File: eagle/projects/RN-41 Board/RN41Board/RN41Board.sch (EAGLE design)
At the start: 16 parts, among them J1 640456-5, Q1 MOSFET-NCHANNELSMD, U1 BLUETOOTH-RN41, U3 3.3V

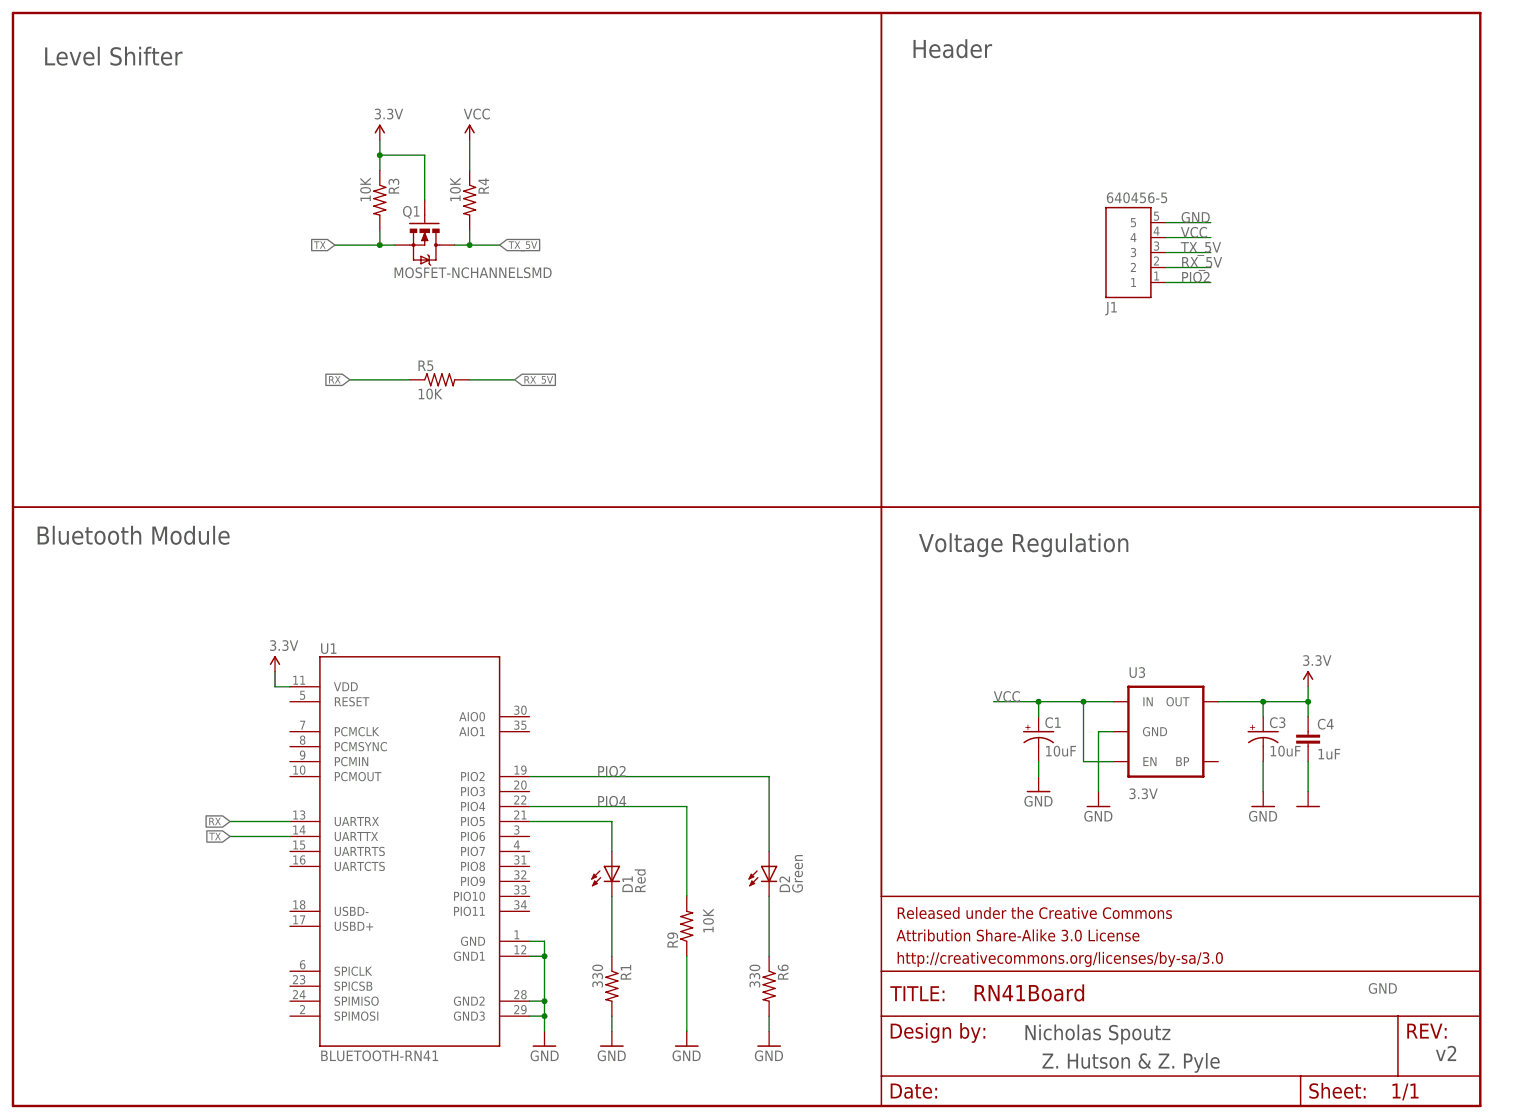
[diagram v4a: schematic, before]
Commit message: OSHPark .dru and RN-41 Update
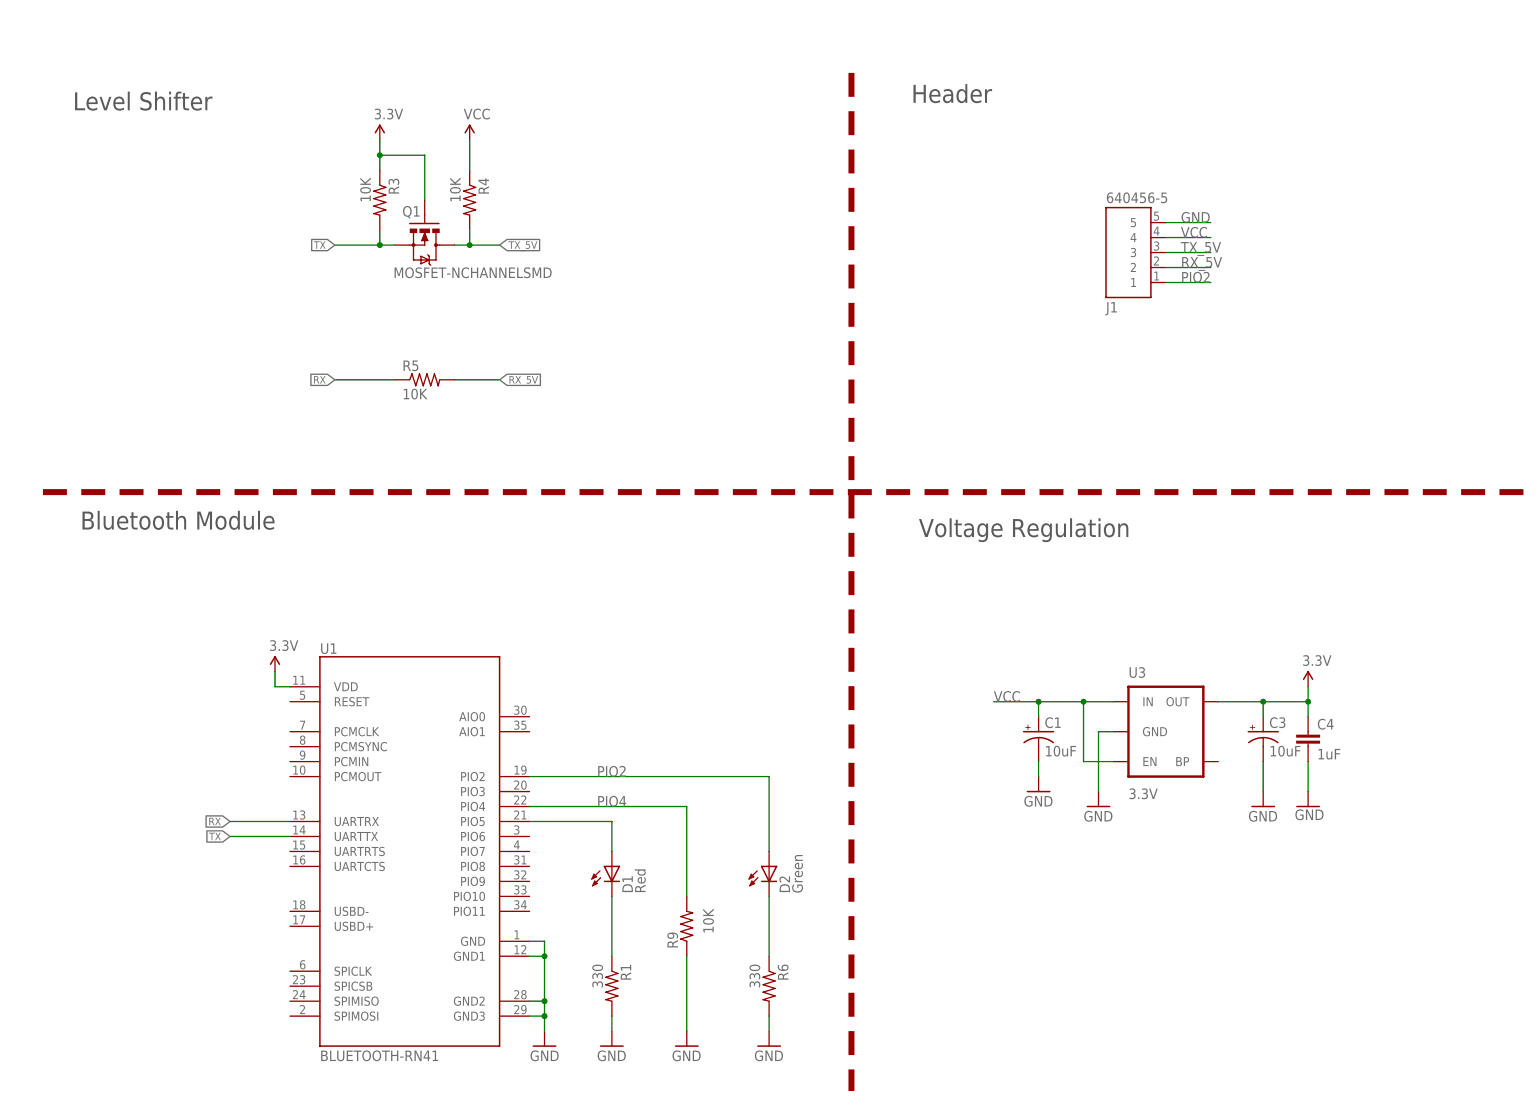
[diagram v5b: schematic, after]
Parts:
- removed FRAME1: FRAME-LETTER, SparkFun-Aesthetics:FRAME-LETTER
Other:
- note removed: "Nicholas Spoutz"
- note removed: "Z. Hutson & Z. Pyle"
- note removed: "v2"
- moved on the sheet: R5
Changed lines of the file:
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@@
 <?xml version="1.0" encoding="utf-8"?>
 <!DOCTYPE eagle SYSTEM "eagle.dtd">
-<eagle version="9.3.0">
+<eagle version="9.3.1">
 <drawing>
 <settings>
@@
 <setting verticaltext="up"/>
 </settings>
-<grid distance="0.1" unitdist="inch" unit="inch" style="lines" multiple="1" display="no" altdistance="0.01" altunitdist="inch" altunit="inch"/>
+<grid distance="0.1" unitdist="inch" unit="inch" style="lines" multiple="1" display="yes" altdistance="0.01" altunitdist="inch" altunit="inch"/>
 <layers>
 <layer number="1" name="Top" color="4" fill="1" visible="no" active="no"/>
@@
 </classes>
 <parts>
-<part name="FRAME1" library="SparkFun-Aesthetics" deviceset="FRAME-LETTER" device=""/>
 <part name="C4" library="SparkFun" deviceset="CAP" device="0603-CAP" value="1uF"/>
 <part name="GND1" library="SparkFun" deviceset="GND" device=""/>
@@
 <part name="GND8" library="SparkFun" deviceset="GND" device=""/>
 <part name="J1" library="640456-5" deviceset="640456-5" device=""/>
+<part name="FRAME2" library="frames" library_urn="urn:adsk.eagle:library:229" deviceset="A4L-LOC" device=""/>
 </parts>
 <sheets>
 <sheet>
 <plain>
-<text x="5.08" y="176.53" size="3.048" layer="97">Level Shifter</text>
-<text x="152.4" y="177.8" size="3.048" layer="97">Header</text>
-<text x="171.45" y="11.176" size="2.54" layer="97">Nicholas Spoutz</text>
-<text x="241.3" y="7.62" size="2.54" layer="97">v2</text>
-<text x="174.498" y="6.35" size="2.54" layer="97">Z. Hutson &amp; Z. Pyle</text>
-<wire x1="0" y1="101.6" x2="248.92" y2="101.6" width="0.3048" layer="94"/>
-<wire x1="147.32" y1="35.56" x2="147.32" y2="185.42" width="0.3048" layer="94"/>
-<text x="153.67" y="93.98" size="3.048" layer="97">Voltage Regulation</text>
-<text x="3.81" y="95.25" size="3.048" layer="97">Bluetooth Module</text>
+<text x="10.16" y="168.91" size="3.048" layer="97">Level Shifter</text>
+<text x="152.4" y="170.18" size="3.048" layer="97">Header</text>
+<text x="153.67" y="96.52" size="3.048" layer="97">Voltage Regulation</text>
+<text x="11.43" y="97.79" size="3.048" layer="97">Bluetooth Module</text>
+<wire x1="5.08" y1="104.14" x2="256.54" y2="104.14" width="1.016" layer="94" style="dashdot"/>
+<wire x1="142.24" y1="175.26" x2="142.24" y2="2.54" width="1.016" layer="94" style="dashdot"/>
 </plain>
 <instances>
-<instance part="FRAME1" gate="G$1" x="0" y="0" smashed="yes"/>
-<instance part="FRAME1" gate="G$2" x="147.32" y="0" smashed="yes">
-<attribute name="LAST_DATE_TIME" x="160.02" y="1.27" size="2.54" layer="94" font="vector"/>
-<attribute name="SHEET" x="233.68" y="1.27" size="2.54" layer="94" font="vector"/>
-<attribute name="DRAWING_NAME" x="162.814" y="17.78" size="2.7432" layer="94" font="vector"/>
-</instance>
 <instance part="C4" gate="G$1" x="219.71" y="60.96" smashed="yes">
 <attribute name="NAME" x="221.234" y="63.881" size="1.778" layer="95"/>
@@
 </instance>
 <instance part="GND3" gate="1" x="219.71" y="50.8" smashed="yes">
-<attribute name="VALUE" x="229.87" y="19.05" size="1.778" layer="96"/>
+<attribute name="VALUE" x="217.424" y="48.514" size="1.778" layer="96"/>
 </instance>
 <instance part="P+2" gate="1" x="219.71" y="71.12" smashed="yes">
@@
 <attribute name="VALUE" x="76.454" y="167.386" size="1.778" layer="96"/>
 </instance>
-<instance part="R5" gate="G$1" x="72.39" y="123.19" smashed="yes">
-<attribute name="NAME" x="68.58" y="124.6886" size="1.778" layer="95"/>
-<attribute name="VALUE" x="68.58" y="119.888" size="1.778" layer="96"/>
+<instance part="R5" gate="G$1" x="69.85" y="123.19" smashed="yes">
+<attribute name="NAME" x="66.04" y="124.6886" size="1.778" layer="95"/>
+<attribute name="VALUE" x="66.04" y="119.888" size="1.778" layer="96"/>
 </instance>
 <instance part="P+5" gate="1" x="44.45" y="73.66" smashed="yes">
@@
 <attribute name="NAME" x="185.414740625" y="136.38931875" size="1.779840625" layer="95" rot="MR180"/>
 <attribute name="VALUE" x="185.411040625" y="154.9579" size="1.781140625" layer="96" rot="MR180"/>
+</instance>
+<instance part="FRAME2" gate="G$1" x="0" y="0" smashed="yes">
+<attribute name="DRAWING_NAME" x="217.17" y="15.24" size="2.54" layer="94"/>
+<attribute name="LAST_DATE_TIME" x="217.17" y="10.16" size="2.286" layer="94"/>
+<attribute name="SHEET" x="230.505" y="5.08" size="2.54" layer="94"/>
 </instance>
 </instances>
@@
 <net name="RX" class="0">
 <segment>
-<wire x1="67.31" y1="123.19" x2="57.15" y2="123.19" width="0.1524" layer="91"/>
+<wire x1="64.77" y1="123.19" x2="54.61" y2="123.19" width="0.1524" layer="91"/>
 <pinref part="R5" gate="G$1" pin="1"/>
-<label x="57.15" y="123.19" size="1.27" layer="95" rot="R180" xref="yes"/>
+<label x="54.61" y="123.19" size="1.27" layer="95" rot="R180" xref="yes"/>
 </segment>
 <segment>
@@
 <net name="RX_5V" class="0">
 <segment>
-<wire x1="77.47" y1="123.19" x2="85.09" y2="123.19" width="0.1524" layer="91"/>
+<wire x1="74.93" y1="123.19" x2="82.55" y2="123.19" width="0.1524" layer="91"/>
 <pinref part="R5" gate="G$1" pin="2"/>
-<label x="85.09" y="123.19" size="1.27" layer="95" xref="yes"/>
+<label x="82.55" y="123.19" size="1.27" layer="95" xref="yes"/>
 </segment>
 <segment>
@@
 </schematic>
 </drawing>
+<compatibility>
+<note version="8.2" severity="warning">
+Since Version 8.2, EAGLE supports online libraries. The ids
+of those online libraries will not be understood (or retained)
+with this version.
+</note>
+<note version="8.3" severity="warning">
+Since Version 8.3, EAGLE supports URNs for individual library
+assets (packages, symbols, and devices). The URNs of those assets
+will not be understood (or retained) with this version.
+</note>
+</compatibility>
 </eagle>

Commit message: Update
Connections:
- net RX_5V: now also J1.3; no longer J1.2
- net TX_5V: now also J1.2; no longer J1.3
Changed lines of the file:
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@@
 <setting verticaltext="up"/>
 </settings>
-<grid distance="0.1" unitdist="inch" unit="inch" style="lines" multiple="1" display="yes" altdistance="0.01" altunitdist="inch" altunit="inch"/>
+<grid distance="0.1" unitdist="inch" unit="inch" style="lines" multiple="1" display="no" altdistance="0.01" altunitdist="inch" altunit="inch"/>
 <layers>
 <layer number="1" name="Top" color="4" fill="1" visible="no" active="no"/>
@@
 </segment>
 <segment>
+<pinref part="J1" gate="G$1" pin="2"/>
+<wire x1="195.58" y1="142.24" x2="203.2" y2="142.24" width="0.1524" layer="91"/>
+<label x="198.12" y="142.24" size="1.778" layer="95"/>
+</segment>
+</net>
+<net name="D1" class="0">
+<segment>
+<wire x1="101.6" y1="35.56" x2="101.6" y2="25.4" width="0.1524" layer="91"/>
+<pinref part="R1" gate="G$1" pin="1"/>
+<pinref part="D1" gate="G$1" pin="C"/>
+</segment>
+</net>
+<net name="RX" class="0">
+<segment>
+<wire x1="64.77" y1="123.19" x2="54.61" y2="123.19" width="0.1524" layer="91"/>
+<pinref part="R5" gate="G$1" pin="1"/>
+<label x="54.61" y="123.19" size="1.27" layer="95" rot="R180" xref="yes"/>
+</segment>
+<segment>
+<wire x1="46.99" y1="48.26" x2="36.83" y2="48.26" width="0.1524" layer="91"/>
+<pinref part="U1" gate="G$1" pin="UARTRX"/>
+<label x="36.83" y="48.26" size="1.27" layer="95" rot="R180" xref="yes"/>
+</segment>
+</net>
+<net name="RX_5V" class="0">
+<segment>
+<wire x1="74.93" y1="123.19" x2="82.55" y2="123.19" width="0.1524" layer="91"/>
+<pinref part="R5" gate="G$1" pin="2"/>
+<label x="82.55" y="123.19" size="1.27" layer="95" xref="yes"/>
+</segment>
+<segment>
 <pinref part="J1" gate="G$1" pin="3"/>
 <wire x1="195.58" y1="144.78" x2="203.2" y2="144.78" width="0.1524" layer="91"/>
@@
 </segment>
 </net>
-<net name="D1" class="0">
-<segment>
-<wire x1="101.6" y1="35.56" x2="101.6" y2="25.4" width="0.1524" layer="91"/>
-<pinref part="R1" gate="G$1" pin="1"/>
-<pinref part="D1" gate="G$1" pin="C"/>
-</segment>
-</net>
-<net name="RX" class="0">
-<segment>
-<wire x1="64.77" y1="123.19" x2="54.61" y2="123.19" width="0.1524" layer="91"/>
-<pinref part="R5" gate="G$1" pin="1"/>
-<label x="54.61" y="123.19" size="1.27" layer="95" rot="R180" xref="yes"/>
-</segment>
-<segment>
-<wire x1="46.99" y1="48.26" x2="36.83" y2="48.26" width="0.1524" layer="91"/>
-<pinref part="U1" gate="G$1" pin="UARTRX"/>
-<label x="36.83" y="48.26" size="1.27" layer="95" rot="R180" xref="yes"/>
-</segment>
-</net>
-<net name="RX_5V" class="0">
-<segment>
-<wire x1="74.93" y1="123.19" x2="82.55" y2="123.19" width="0.1524" layer="91"/>
-<pinref part="R5" gate="G$1" pin="2"/>
-<label x="82.55" y="123.19" size="1.27" layer="95" xref="yes"/>
-</segment>
-<segment>
-<pinref part="J1" gate="G$1" pin="2"/>
-<wire x1="195.58" y1="142.24" x2="203.2" y2="142.24" width="0.1524" layer="91"/>
-<label x="198.12" y="142.24" size="1.778" layer="95"/>
-</segment>
-</net>

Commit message: Cap Update
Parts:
- added 3.3V: TEST-POINTPOGO_PTH, SparkFun-Connectors:TEST-POINTPOGO_PTH
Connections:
- net 3.3V: now also 3.3V.1
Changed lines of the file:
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@@
 <part name="J1" library="640456-5" deviceset="640456-5" device=""/>
 <part name="FRAME2" library="frames" library_urn="urn:adsk.eagle:library:229" deviceset="A4L-LOC" device=""/>
+<part name="3.3V" library="SparkFun-Connectors" deviceset="TEST-POINT" device="POGO_PTH"/>
 </parts>
 <sheets>
@@
 <attribute name="LAST_DATE_TIME" x="217.17" y="10.16" size="2.286" layer="94"/>
 <attribute name="SHEET" x="230.505" y="5.08" size="2.54" layer="94"/>
+</instance>
+<instance part="3.3V" gate="G$1" x="226.06" y="68.58" smashed="yes">
+<attribute name="NAME" x="223.52" y="71.12" size="1.778" layer="95" font="vector"/>
+<attribute name="VALUE" x="223.52" y="66.04" size="1.778" layer="96" font="vector"/>
 </instance>
 </instances>
@@
 <segment>
 <wire x1="204.47" y1="68.58" x2="212.09" y2="68.58" width="0.1524" layer="91"/>
-<wire x1="212.09" y1="68.58" x2="219.71" y2="68.58" width="0.1524" layer="91"/>
+<wire x1="212.09" y1="68.58" x2="218.44" y2="68.58" width="0.1524" layer="91"/>
+<wire x1="218.44" y1="68.58" x2="219.71" y2="68.58" width="0.1524" layer="91"/>
 <wire x1="219.71" y1="68.58" x2="219.71" y2="66.04" width="0.1524" layer="91"/>
 <wire x1="219.71" y1="68.58" x2="219.71" y2="71.12" width="0.1524" layer="91"/>
@@
 <pinref part="U3" gate="G$1" pin="OUT"/>
 <pinref part="C3" gate="G$1" pin="+"/>
-</segment>
-<segment>
+<pinref part="3.3V" gate="G$1" pin="1"/>
+<wire x1="226.06" y1="68.58" x2="219.71" y2="68.58" width="0.1524" layer="91"/>
+</segment>
+<segment>
